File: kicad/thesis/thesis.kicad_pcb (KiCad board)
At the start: 2 copper layers, 100 x 75 mm, 31 parts, among them J1 Conn_01x02_Socket, J10 Conn_01x01_Socket, J11 Conn_01x05_Socket, J12 INA219, J13 12V, J2 Conn_01x05_Socket, J3 Conn_01x07_Socket, J4 Conn_01x04_Socket, J7 Conn_01x01_Socket, J8 Conn_01x01_Socket, J9 Conn_01x03_Socket, Q1 IRLZB8721

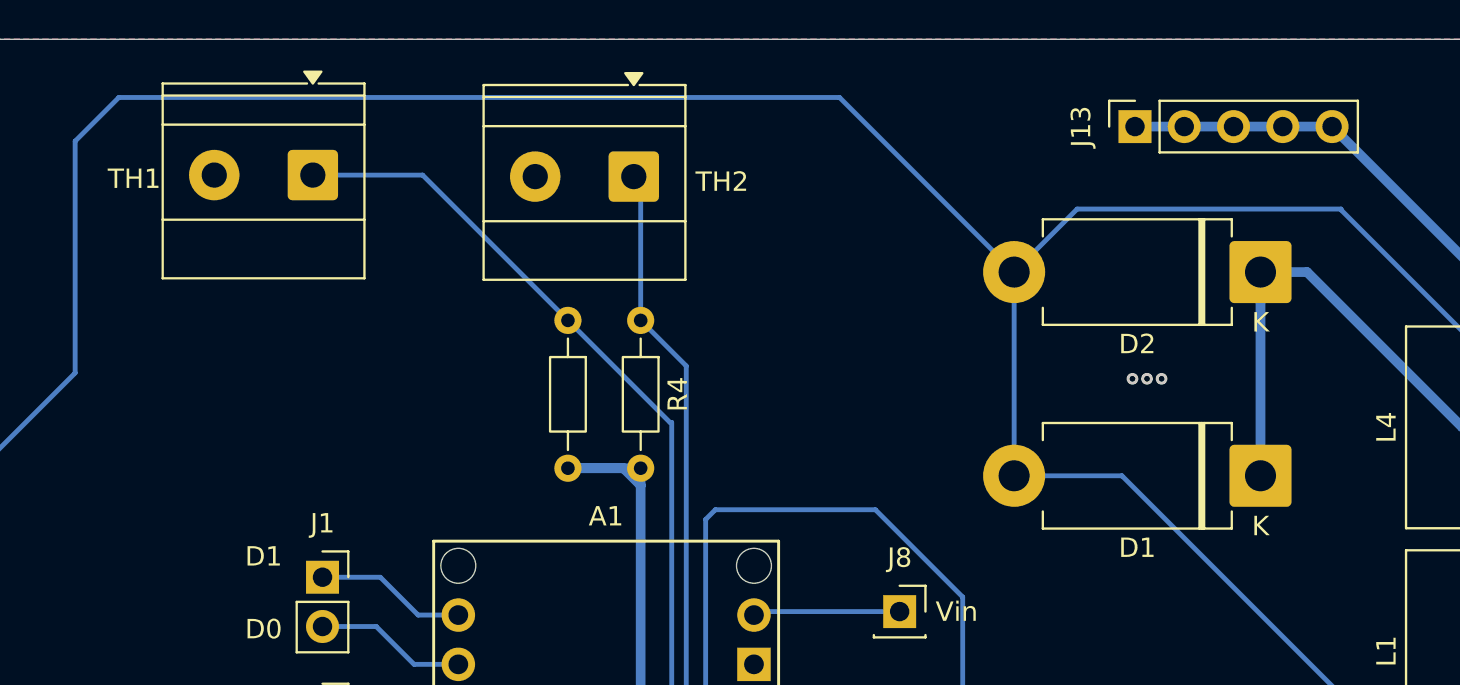
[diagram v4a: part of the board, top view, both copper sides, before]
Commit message: change diode length
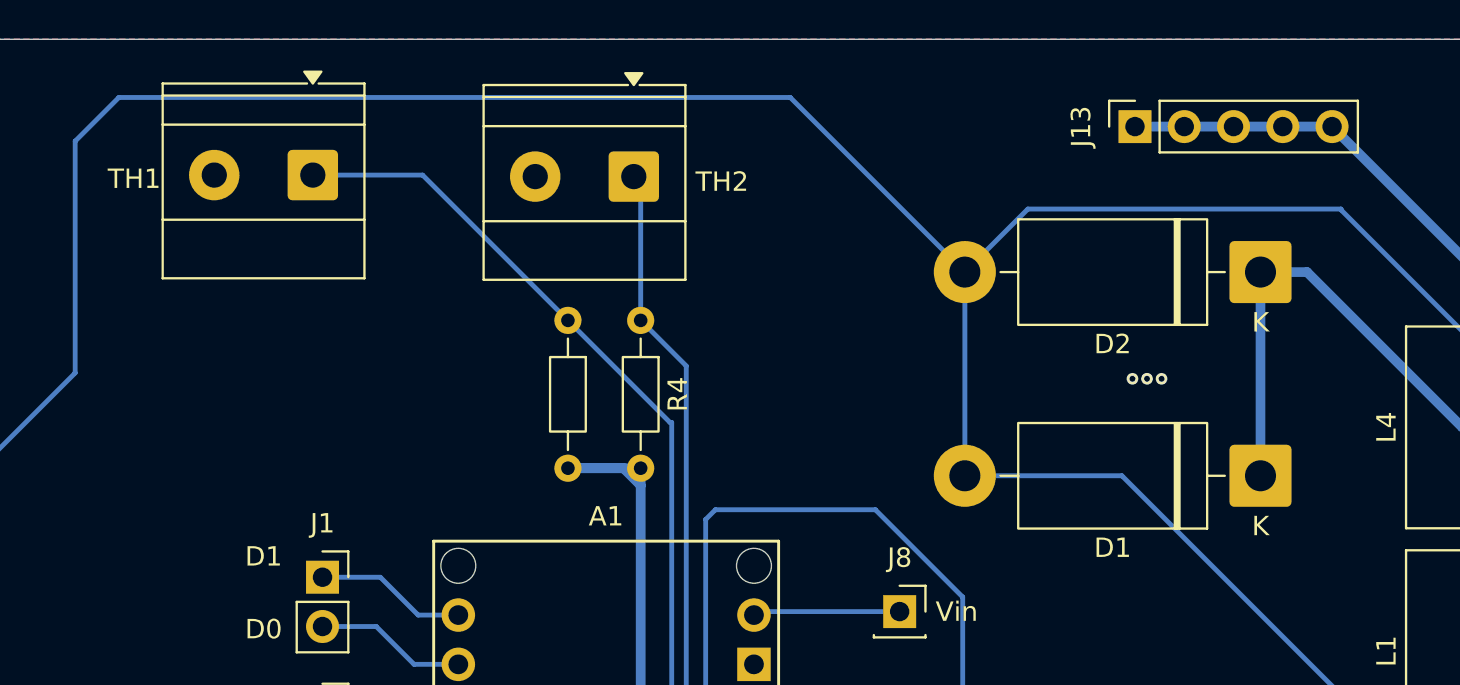
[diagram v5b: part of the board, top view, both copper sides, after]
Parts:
- D1, D2: footprint Diode_THT:D_DO-201AD_P12.70mm_Horizontal -> Diode_THT:D_DO-201AD_P15.24mm_Horizontal
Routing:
- net Net-(D1-A): track 150.1 -> 152.7 mm
